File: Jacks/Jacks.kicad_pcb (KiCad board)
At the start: 2 copper layers, 45 x 27.5 mm, 42 parts, among them J101 Barrel_Jack_Switch, J102 AudioJack2_Ground, J103 AudioJack2_Ground, J104 Conn_02x05_Odd_Even, Q101 DMC3071LVT, Q102 BC846, Q201 LS844, Q301 DMC3071LVT, Q302 DMC3071LVT

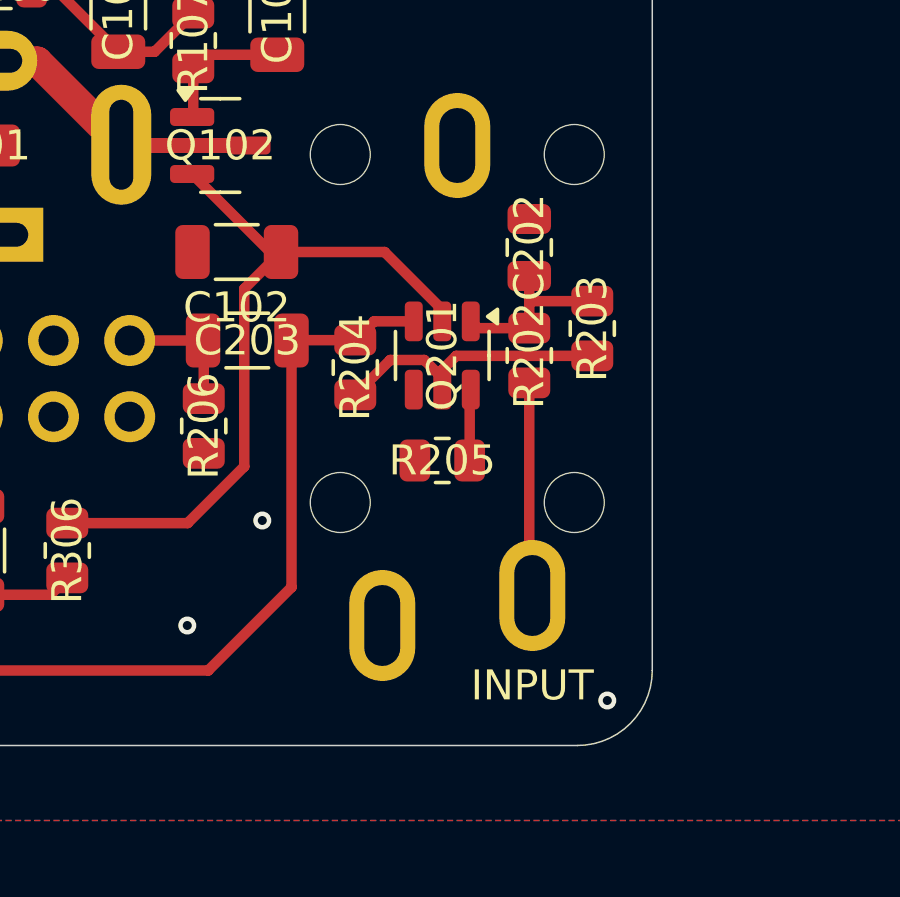
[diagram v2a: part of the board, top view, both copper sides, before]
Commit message: Don't DC-couple the LS844 JFET input
I didn't think this through: it looks superficially fine only because
the circuit doesn't make the _other_ side of the JFET gate connection
obvious.

Without the AC-coupling capacitor, the input gate of the LS844 now has a
relatively low impedance path to ground, going through the instrument.
So the self-biasing to ground with a high-value resistor doesn't work at
all.

To do DC coupling, I'd need an actual negative rail.  I technically knew
that, but I clearly hadn't really internalized it and so just overlooked
this obvious (in hindsight) fact entirely.

I do have the simulation infrastructure for this and when you look at
the results you see that the biasing is all wrong without the
DC-blocking capacitor in place.

But to see that you do need to look at it, and I hadn't bothered since
it all used to work fine and I didn't think about this.

Signed-off-by: Linus Torvalds <torvalds@linux-foundation.org>
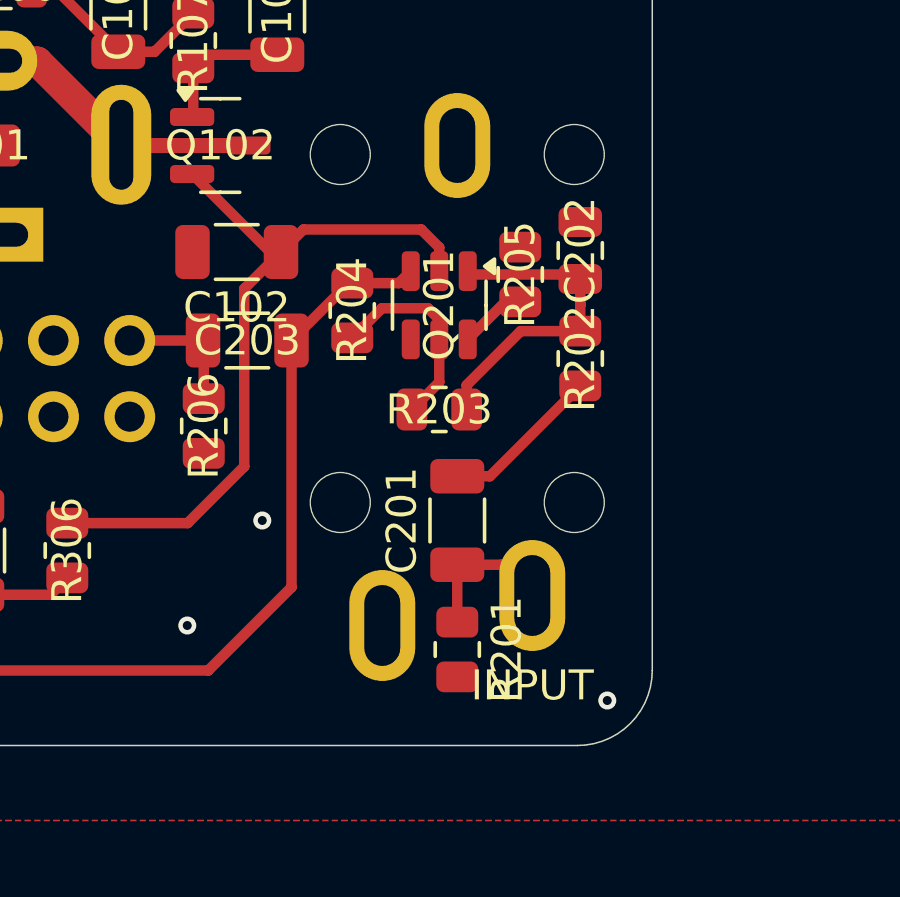
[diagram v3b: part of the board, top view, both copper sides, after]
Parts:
- added C201: 4.7uF, Capacitor_SMD:C_1206_3216Metric, F.Cu at (116.0, 62.5)
- added R201: 1MEG, Resistor_SMD:R_0805_2012Metric, F.Cu at (116.0, 66.8)
- moved R205 6.72 mm to (118.1, 54.3), turned to 90 degrees
- moved R203 5.77 mm to (115.4, 58.8), turned to 180 degrees
- moved R204 1.90 mm to (112.5, 55.5)
- moved C202 1.70 mm to (120.1, 53.5)
- moved R202 1.70 mm to (120.1, 57.1)
- moved Q201 1.68 mm to (115.4, 55.3)
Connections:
- R202 pad 1: IN^{CONN} -> Net-(C201-Pad2)
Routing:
- net Net-(C201-Pad2): track 0.00 -> 5.35 mm
- net Net-(Q201A-G): track 5.89 -> 11.0 mm
- net Net-(Q201B-D): track 9.87 -> 6.84 mm
- net IN^{CONN}: track 7.82 -> 5.53 mm
- net BUFFERED: track 39.6 -> 40.2 mm
